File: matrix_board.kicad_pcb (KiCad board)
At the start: 2 copper layers, 8 parts, among them J1 MATRIX_CONNECTOR, M1 PWR_LED, M2 LED, U1 ATmega328P-AU

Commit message: commit before milling
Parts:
- J1: footprint Connector_PinHeader_2.00mm:PinHeader_2x08_P2.00mm_Vertical_SMD -> fab:fab-2X16SMD
- U1: footprint Package_QFP:TQFP-32_7x7mm_P0.8mm -> fab:fab-TQFP32-08THIN
- moved M2 19.3 mm to (143.5, 77.6)
- moved R2 18.3 mm to (140.6, 77.6)
- moved J1 7.73 mm to (157.1, 77.2)
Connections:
- J1 pad 16: GND -> GROUND
- U1 pad 1: R2 -> G1
- U1 pad 10: OE -> G2
- U1 pad 12: Net-(U1-Pad12) -> CLK
- U1 pad 13: Net-(U1-Pad13) -> OE
- U1 pad 14: TEST -> LAT
- U1 pad 2: G2 -> B1
- U1 pad 27: Net-(U1-Pad27) -> TEST
- U1 pad 30: R1 -> Net-(U1-Pad30)
- U1 pad 31: G1 -> Net-(U1-Pad31)
- U1 pad 32: B1 -> R1
- U1 pad 7: CLK -> Net-(U1-Pad7)
- U1 pad 9: LAT -> R2
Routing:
- net GROUND: track 16.5 -> 145.0 mm, vias 0 -> 3
- net TEST: track 3.86 -> 76.6 mm, vias 0 -> 2
- net VCC: track 15.9 -> 49.3 mm, vias 0 -> 2
- net LAT: track 12.2 -> 33.2 mm
- net A: track 26.4 -> 41.8 mm
- net G2: track 11.5 -> 20.9 mm
- net R2: track 16.5 -> 25.3 mm
- net CLK: track 16.6 -> 23.5 mm
- net C: track 28.2 -> 34.7 mm
- net B2: track 31.9 -> 25.8 mm
- net B: track 22.7 -> 26.4 mm
- net OE: track 19.3 -> 22.4 mm
- net G1: track 15.1 -> 12.3 mm
- net MISO: track 17.4 -> 15.1 mm
- net R1: track 21.3 -> 19.1 mm
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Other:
- board outline added: 48.3 x 26 mm
- net class Default: clearance 0.3 -> 0.4
- rule trace_clearance: 0.3 -> 0.4

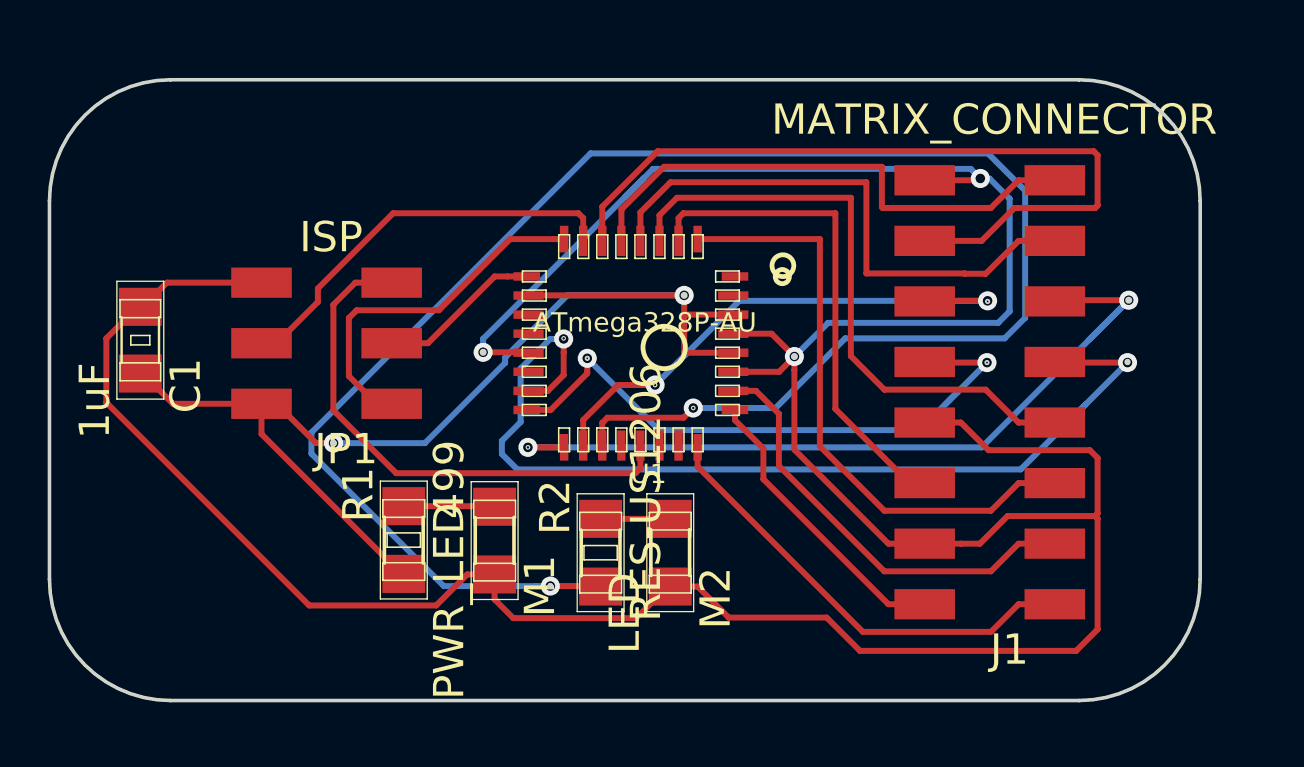
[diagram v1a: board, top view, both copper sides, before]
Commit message: added more accurate rivets
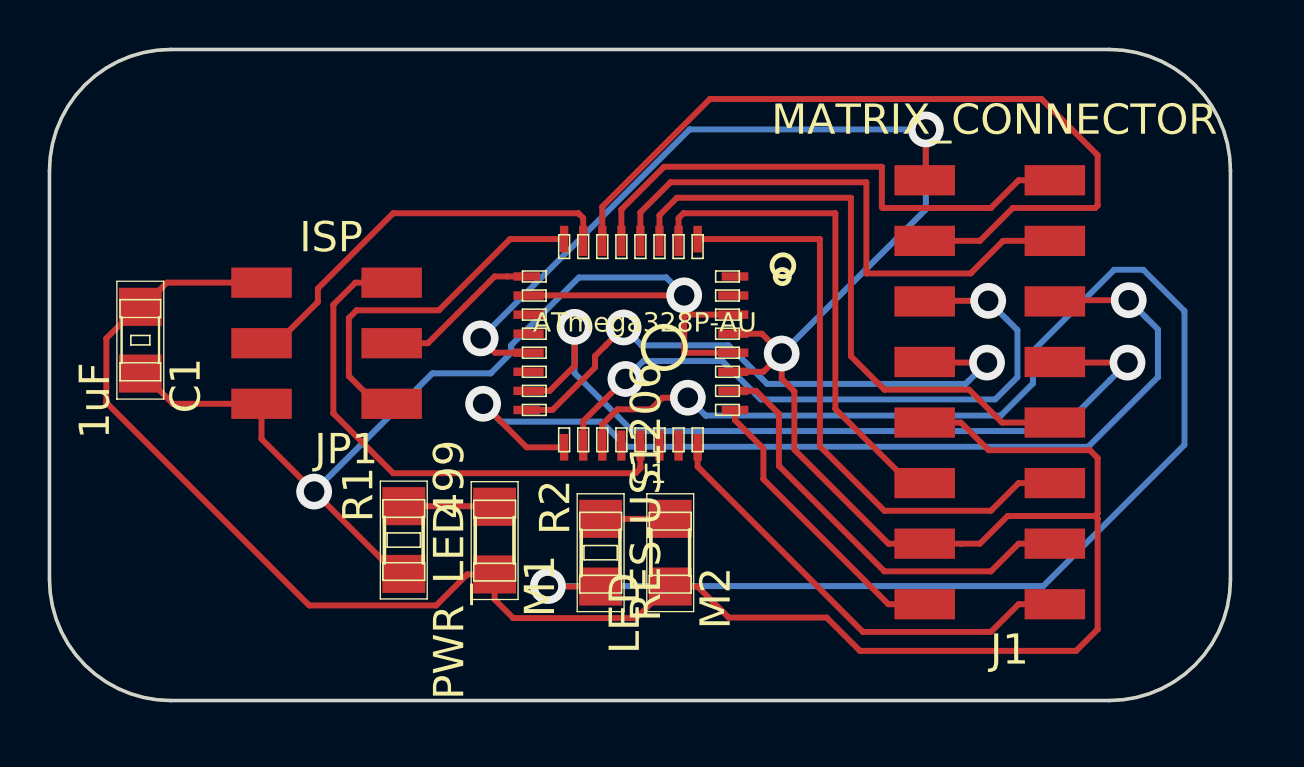
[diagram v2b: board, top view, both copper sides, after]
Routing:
- net TEST: track 76.6 -> 67.1 mm
- net GROUND: track 145.0 -> 136.8 mm
- net A: track 41.8 -> 34.4 mm
- net C: track 34.7 -> 41.3 mm
- net D: track 22.8 -> 27.7 mm
- net LAT: track 33.2 -> 35.0 mm
- net B: track 26.4 -> 25.0 mm
- net VCC: track 49.3 -> 48.2 mm
- net RESET: track 22.3 -> 22.9 mm
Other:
- board size 48.3 x 26 mm -> 49.5 x 27.3 mm

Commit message: added new board design. hope it works
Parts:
- added S1: PD0_SWITCH, fab:fab-6MM_SWITCH, F.Cu at (148.3, 55.9)
- added S2: PD1_SWITCH, fab:fab-6MM_SWITCH, F.Cu at (137.7, 55.9)
- C1: footprint kicad_fab:fab-C1206 -> fab:fab-C1206
- J1: footprint fab:fab-2X16SMD -> Connector_PinHeader_2.00mm:PinHeader_2x08_P2.00mm_Vertical_SMD
- JP1: footprint kicad_fab:fab-2X03SMD -> fab:fab-2X03SMD
- M1, M2: footprint kicad_fab:fab-LED1206 -> fab:fab-LED1206
- R1, R2: footprint kicad_fab:fab-R1206 -> fab:fab-R1206
- moved C1 51.9 mm to (173.1, 65.0), turned to 0 degrees
- moved JP1 51.7 mm to (181.0, 68.1), turned to 0 degrees
- moved R1 41.3 mm to (169.2, 58.4), turned to 0 degrees
- moved M1 41.1 mm to (169.3, 52.8), turned to 0 degrees
- moved R2 26.5 mm to (161.1, 61.0), turned to 0 degrees
- moved J1 26.4 mm to (131.1, 73.2), turned to 0 degrees
- moved M2 21.5 mm to (160.9, 65.0), turned to 0 degrees
- moved U1 16.5 mm to (157.5, 74.2), turned to 0 degrees
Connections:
- U1 pad 30: Net-(U1-Pad30) -> PD0
- U1 pad 31: Net-(U1-Pad31) -> PD1
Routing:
- net GROUND: track 136.8 -> 245.3 mm
- net VCC: track 48.2 -> 115.1 mm
- net TEST: track 67.1 -> 9.67 mm, vias 2 -> 0
- net PD1: track 0.00 -> 34.2 mm
- net PD0: track 0.00 -> 24.3 mm
- net A: track 34.4 -> 52.7 mm
- net SCK: track 7.46 -> 25.1 mm
- net MISO: track 15.1 -> 30.8 mm
- net MOSI: track 17.1 -> 31.3 mm
- net B: track 25.0 -> 38.5 mm
- net RESET: track 22.9 -> 35.6 mm
- net C: track 41.3 -> 53.9 mm
- net OE: track 22.4 -> 34.3 mm
- net LAT: track 35.0 -> 46.4 mm
- net D: track 27.7 -> 38.1 mm
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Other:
- board size 49.5 x 27.3 mm -> 71.1 x 45.7 mm
- net class Default: clearance 0.4 -> 0.3; via_dia 0.8 -> 1.6; via_drill 0.4 -> 0.89
- rule pad_to_mask_clearance: 0.051 -> 0
- rule trace_clearance: 0.4 -> 0.3

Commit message: remade board to be bigger
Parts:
- added M3: PINHD-2X2-SMD, fab:fab-2X02SMD, F.Cu at (162.1, 53.3)
- moved C1 1.83 mm to (174.6, 64.0)
- moved J1 1.83 mm to (132.6, 72.1)
- moved JP1 1.83 mm to (182.5, 67.1)
- moved M2 1.83 mm to (162.5, 64.0)
- moved S1 1.83 mm to (149.9, 54.9)
- moved S2 1.83 mm to (139.2, 54.9)
- moved U1 1.83 mm to (159.0, 73.2)
- moved M1 1.83 mm to (170.8, 51.8)
- moved R1 1.83 mm to (170.7, 57.4)
- moved R2 1.83 mm to (162.7, 59.9)
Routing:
- net VCC: track 115.1 -> 105.0 mm
- net GROUND: track 245.3 -> 251.5 mm
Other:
- board size 71.1 x 45.7 mm -> 68.1 x 40.1 mm

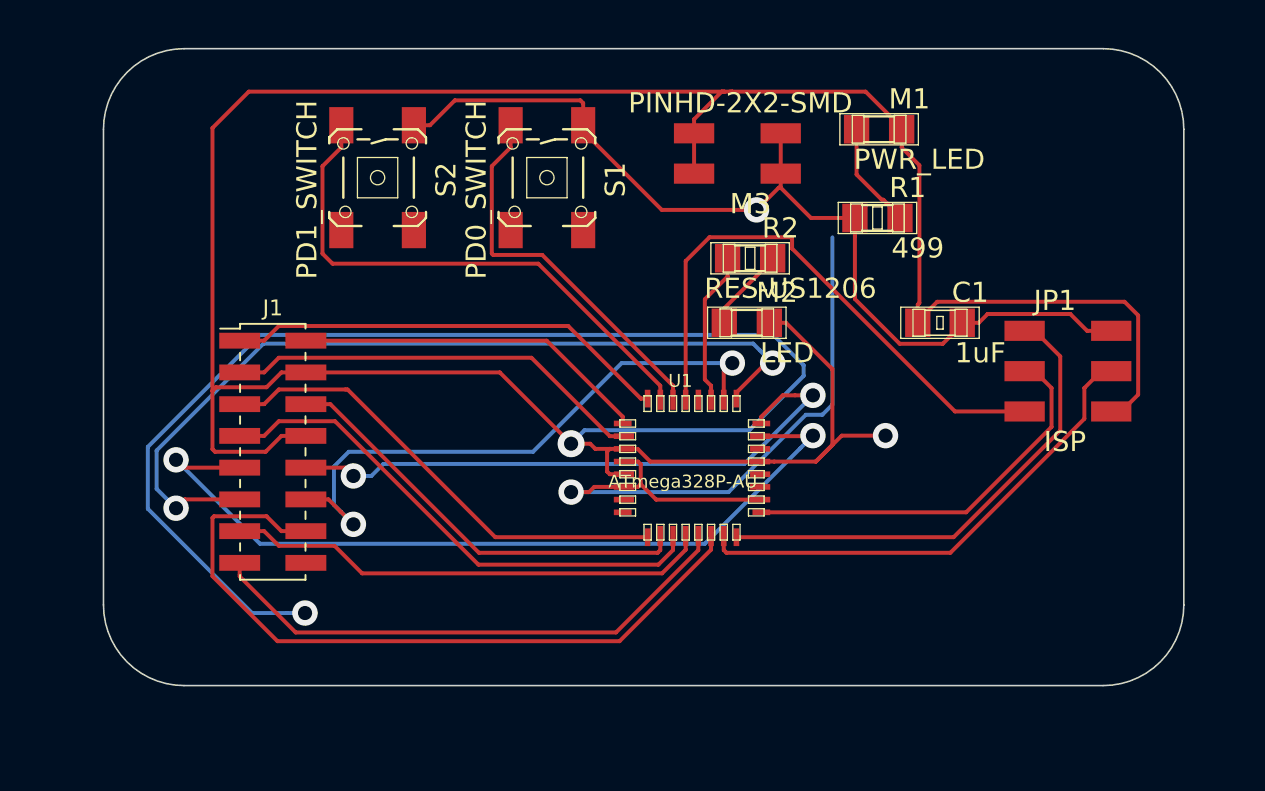
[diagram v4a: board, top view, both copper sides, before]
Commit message: updated board with more components so it'll work
added pull up resistor on reset and clock on xtal, also moved capacitor closer to chip
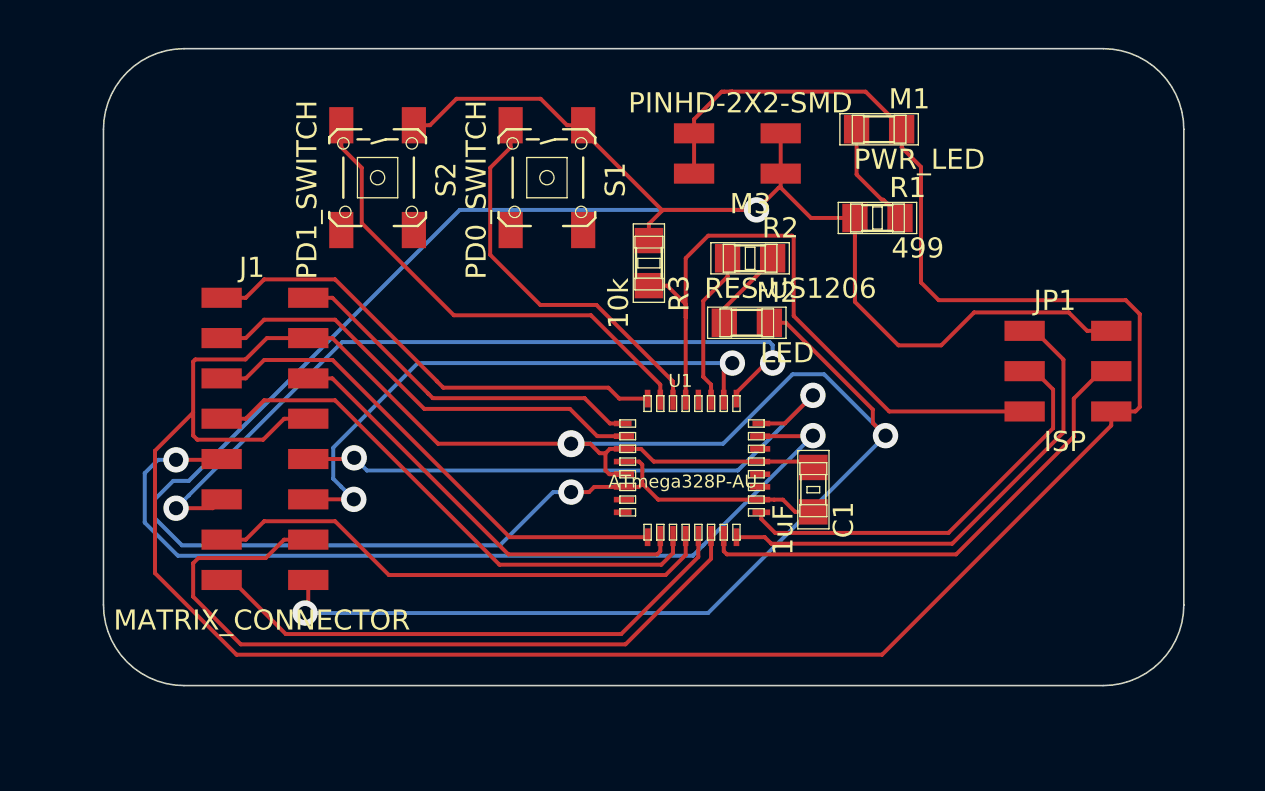
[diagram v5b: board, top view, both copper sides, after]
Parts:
- added R3: 10k, fab:fab-R1206, F.Cu at (156.3, 60.2)
- J1: footprint Connector_PinHeader_2.00mm:PinHeader_2x08_P2.00mm_Vertical_SMD -> fab:fab-2X08SMD
- moved C1 13.2 mm to (166.6, 74.5), turned to 270 degrees
- moved J1 7.20 mm to (131.9, 65.0)
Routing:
- net VCC: track 105.0 -> 156.2 mm
- net GROUND: track 251.5 -> 267.0 mm
- net RESET: track 35.6 -> 42.0 mm
- net A: track 52.7 -> 57.8 mm
- net C: track 53.9 -> 49.7 mm
- net PD1: track 34.2 -> 30.7 mm
- net R1: track 28.0 -> 30.4 mm
- net B1: track 26.6 -> 28.9 mm
- net CLK: track 30.7 -> 32.8 mm
- net R2: track 29.9 -> 31.9 mm
- net B2: track 32.7 -> 34.6 mm
- net D: track 38.1 -> 36.6 mm
- net SCK: track 25.1 -> 26.6 mm
- net LAT: track 46.4 -> 47.5 mm
- net G1: track 22.4 -> 23.1 mm
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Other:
- net class Default: clearance 0.3 -> 0.4
- rule trace_clearance: 0.3 -> 0.4
